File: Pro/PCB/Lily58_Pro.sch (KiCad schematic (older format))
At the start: 83 parts, among them J1 LED, J2 4PIN, J3 OLED, P1 i2c_pin, P2 i2c_pin, SW1 SW_PUSH, SW10 SW_PUSH, SW11 SW_PUSH, SW12 SW_PUSH, SW13 SW_PUSH, SW14 SW_PUSH, SW15 SW_PUSH, SW16 SW_PUSH, SW17 SW_PUSH, SW18 SW_PUSH, SW19 SW_PUSH, SW2 SW_PUSH, SW20 SW_PUSH, SW21 SW_PUSH, SW22 SW_PUSH, SW23 SW_PUSH, SW24 SW_PUSH, SW25 SW_PUSH, SW26 SW_PUSH, SW27 SW_PUSH, SW28 SW_PUSH, SW29 SW_PUSH, SW3 SW_PUSH, SW4 SW_PUSH, SW5 SW_PUSH, SW6 SW_PUSH, SW7 SW_PUSH, SW8 SW_PUSH, SW9 SW_PUSH, U1 ProMicro

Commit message: Add another switch.
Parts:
- added D30: D, Lily58-footprint:Diode_SOD123, symbol Lily58_Pro-rescue:D-Lily58-cache
- added SW30: SW_PUSH, Lily58-footprint:CherryMX_KailhLowProfile_Hotswap, symbol Lily58_Pro-rescue:SW_PUSH-Lily58-cache
- SW1, SW10, SW11, SW12, SW13, SW14, SW15, SW16, SW17, SW18, SW19, SW2, SW20, SW21, SW22, SW23, SW24, SW25, SW27, SW28, SW29, SW3, SW4, SW5, SW6, SW7, SW8, SW9: footprint Lily58-footprint:CherryMX_KailhLowProfile_Hotswap_edge_fixed -> Lily58-footprint:CherryMX_KailhLowProfile_Hotswap
- SW26: footprint Lily58-footprint:CherryMX_KailhLowProfile_Hotswap_edge_fixed -> Lily58-footprint:CherryMX_KailhLowProfile_Hotswap_1.5
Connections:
- net col0: now also SW30.1
- net row4: now also D30.1 (K)
- new net: D30.2 (A), SW30.2
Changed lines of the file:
@@
 F 0 "SW25" H 5800 5000 50  0000 C CNN
 F 1 "SW_PUSH" H 5800 4750 50  0000 C CNN
-F 2 "Lily58-footprint:CherryMX_KailhLowProfile_Hotswap_edge_fixed" H 5800 4850 50  0001 C CNN
+F 2 "Lily58-footprint:CherryMX_KailhLowProfile_Hotswap" H 5800 4850 50  0001 C CNN
 F 3 "" H 5800 4850 50  0000 C CNN
 	1    5800 4850
@@
 F 0 "SW26" H 6600 5000 50  0000 C CNN
 F 1 "SW_PUSH" H 6600 4750 50  0000 C CNN
-F 2 "Lily58-footprint:CherryMX_KailhLowProfile_Hotswap_edge_fixed" H 6600 4850 50  0001 C CNN
+F 2 "Lily58-footprint:CherryMX_KailhLowProfile_Hotswap_1.5" H 6600 4850 50  0001 C CNN
 F 3 "" H 6600 4850 50  0000 C CNN
 	1    6600 4850
@@
 F 0 "SW1" H 5800 2400 50  0000 C CNN
 F 1 "SW_PUSH" H 5800 2150 50  0000 C CNN
-F 2 "Lily58-footprint:CherryMX_KailhLowProfile_Hotswap_edge_fixed" H 5800 2250 50  0001 C CNN
+F 2 "Lily58-footprint:CherryMX_KailhLowProfile_Hotswap" H 5800 2250 50  0001 C CNN
 F 3 "" H 5800 2250 50  0000 C CNN
 	1    5800 2250
@@
 F 0 "SW2" H 6600 2400 50  0000 C CNN
 F 1 "SW_PUSH" H 6600 2150 50  0000 C CNN
-F 2 "Lily58-footprint:CherryMX_KailhLowProfile_Hotswap_edge_fixed" H 6600 2250 50  0001 C CNN
+F 2 "Lily58-footprint:CherryMX_KailhLowProfile_Hotswap" H 6600 2250 50  0001 C CNN
 F 3 "" H 6600 2250 50  0000 C CNN
 	1    6600 2250
@@
 F 0 "SW3" H 7400 2400 50  0000 C CNN
 F 1 "SW_PUSH" H 7400 2150 50  0000 C CNN
-F 2 "Lily58-footprint:CherryMX_KailhLowProfile_Hotswap_edge_fixed" H 7400 2250 50  0001 C CNN
+F 2 "Lily58-footprint:CherryMX_KailhLowProfile_Hotswap" H 7400 2250 50  0001 C CNN
 F 3 "" H 7400 2250 50  0000 C CNN
 	1    7400 2250
@@
 F 0 "SW4" H 8200 2400 50  0000 C CNN
 F 1 "SW_PUSH" H 8200 2150 50  0000 C CNN
-F 2 "Lily58-footprint:CherryMX_KailhLowProfile_Hotswap_edge_fixed" H 8200 2250 50  0001 C CNN
+F 2 "Lily58-footprint:CherryMX_KailhLowProfile_Hotswap" H 8200 2250 50  0001 C CNN
 F 3 "" H 8200 2250 50  0000 C CNN
 	1    8200 2250
@@
 F 0 "SW5" H 9000 2400 50  0000 C CNN
 F 1 "SW_PUSH" H 9000 2150 50  0000 C CNN
-F 2 "Lily58-footprint:CherryMX_KailhLowProfile_Hotswap_edge_fixed" H 9000 2250 50  0001 C CNN
+F 2 "Lily58-footprint:CherryMX_KailhLowProfile_Hotswap" H 9000 2250 50  0001 C CNN
 F 3 "" H 9000 2250 50  0000 C CNN
 	1    9000 2250
@@
 F 0 "SW6" H 9800 2400 50  0000 C CNN
 F 1 "SW_PUSH" H 9800 2200 50  0000 C CNN
-F 2 "Lily58-footprint:CherryMX_KailhLowProfile_Hotswap_edge_fixed" H 9800 2250 50  0001 C CNN
+F 2 "Lily58-footprint:CherryMX_KailhLowProfile_Hotswap" H 9800 2250 50  0001 C CNN
 F 3 "" H 9800 2250 50  0000 C CNN
 	1    9800 2250
@@
 F 0 "SW8" H 6600 3050 50  0000 C CNN
 F 1 "SW_PUSH" H 6600 2800 50  0000 C CNN
-F 2 "Lily58-footprint:CherryMX_KailhLowProfile_Hotswap_edge_fixed" H 6600 2900 50  0001 C CNN
+F 2 "Lily58-footprint:CherryMX_KailhLowProfile_Hotswap" H 6600 2900 50  0001 C CNN
 F 3 "" H 6600 2900 50  0000 C CNN
 	1    6600 2900
@@
 F 0 "SW9" H 7400 3050 50  0000 C CNN
 F 1 "SW_PUSH" H 7400 2800 50  0000 C CNN
-F 2 "Lily58-footprint:CherryMX_KailhLowProfile_Hotswap_edge_fixed" H 7400 2900 50  0001 C CNN
+F 2 "Lily58-footprint:CherryMX_KailhLowProfile_Hotswap" H 7400 2900 50  0001 C CNN
 F 3 "" H 7400 2900 50  0000 C CNN
 	1    7400 2900
@@
 F 0 "SW10" H 8200 3050 50  0000 C CNN
 F 1 "SW_PUSH" H 8200 2800 50  0000 C CNN
-F 2 "Lily58-footprint:CherryMX_KailhLowProfile_Hotswap_edge_fixed" H 8200 2900 50  0001 C CNN
+F 2 "Lily58-footprint:CherryMX_KailhLowProfile_Hotswap" H 8200 2900 50  0001 C CNN
 F 3 "" H 8200 2900 50  0000 C CNN
 	1    8200 2900
@@
 F 0 "SW11" H 9000 3050 50  0000 C CNN
 F 1 "SW_PUSH" H 9000 2800 50  0000 C CNN
-F 2 "Lily58-footprint:CherryMX_KailhLowProfile_Hotswap_edge_fixed" H 9000 2900 50  0001 C CNN
+F 2 "Lily58-footprint:CherryMX_KailhLowProfile_Hotswap" H 9000 2900 50  0001 C CNN
 F 3 "" H 9000 2900 50  0000 C CNN
 	1    9000 2900
@@
 F 0 "SW12" H 9800 3050 50  0000 C CNN
 F 1 "SW_PUSH" H 9800 2800 50  0000 C CNN
-F 2 "Lily58-footprint:CherryMX_KailhLowProfile_Hotswap_edge_fixed" H 9800 2900 50  0001 C CNN
+F 2 "Lily58-footprint:CherryMX_KailhLowProfile_Hotswap" H 9800 2900 50  0001 C CNN
 F 3 "" H 9800 2900 50  0000 C CNN
 	1    9800 2900
@@
 F 0 "SW7" H 5800 3050 50  0000 C CNN
 F 1 "SW_PUSH" H 5800 2800 50  0000 C CNN
-F 2 "Lily58-footprint:CherryMX_KailhLowProfile_Hotswap_edge_fixed" H 5800 2900 50  0001 C CNN
+F 2 "Lily58-footprint:CherryMX_KailhLowProfile_Hotswap" H 5800 2900 50  0001 C CNN
 F 3 "" H 5800 2900 50  0000 C CNN
 	1    5800 2900
@@
 F 0 "SW13" H 5800 3700 50  0000 C CNN
 F 1 "SW_PUSH" H 5800 3450 50  0000 C CNN
-F 2 "Lily58-footprint:CherryMX_KailhLowProfile_Hotswap_edge_fixed" H 5800 3550 50  0001 C CNN
+F 2 "Lily58-footprint:CherryMX_KailhLowProfile_Hotswap" H 5800 3550 50  0001 C CNN
 F 3 "" H 5800 3550 50  0000 C CNN
 	1    5800 3550
@@
 F 0 "SW14" H 6600 3700 50  0000 C CNN
 F 1 "SW_PUSH" H 6600 3450 50  0000 C CNN
-F 2 "Lily58-footprint:CherryMX_KailhLowProfile_Hotswap_edge_fixed" H 6600 3550 50  0001 C CNN
+F 2 "Lily58-footprint:CherryMX_KailhLowProfile_Hotswap" H 6600 3550 50  0001 C CNN
 F 3 "" H 6600 3550 50  0000 C CNN
 	1    6600 3550
@@
 F 0 "SW15" H 7400 3700 50  0000 C CNN
 F 1 "SW_PUSH" H 7400 3450 50  0000 C CNN
-F 2 "Lily58-footprint:CherryMX_KailhLowProfile_Hotswap_edge_fixed" H 7400 3550 50  0001 C CNN
+F 2 "Lily58-footprint:CherryMX_KailhLowProfile_Hotswap" H 7400 3550 50  0001 C CNN
 F 3 "" H 7400 3550 50  0000 C CNN
 	1    7400 3550
@@
 F 0 "SW16" H 8200 3700 50  0000 C CNN
 F 1 "SW_PUSH" H 8200 3450 50  0000 C CNN
-F 2 "Lily58-footprint:CherryMX_KailhLowProfile_Hotswap_edge_fixed" H 8200 3550 50  0001 C CNN
+F 2 "Lily58-footprint:CherryMX_KailhLowProfile_Hotswap" H 8200 3550 50  0001 C CNN
 F 3 "" H 8200 3550 50  0000 C CNN
 	1    8200 3550
@@
 F 0 "SW17" H 9000 3700 50  0000 C CNN
 F 1 "SW_PUSH" H 9000 3450 50  0000 C CNN
-F 2 "Lily58-footprint:CherryMX_KailhLowProfile_Hotswap_edge_fixed" H 9000 3550 50  0001 C CNN
+F 2 "Lily58-footprint:CherryMX_KailhLowProfile_Hotswap" H 9000 3550 50  0001 C CNN
 F 3 "" H 9000 3550 50  0000 C CNN
 	1    9000 3550
@@
 F 0 "SW18" H 9800 3700 50  0000 C CNN
 F 1 "SW_PUSH" H 9800 3450 50  0000 C CNN
-F 2 "Lily58-footprint:CherryMX_KailhLowProfile_Hotswap_edge_fixed" H 9800 3550 50  0001 C CNN
+F 2 "Lily58-footprint:CherryMX_KailhLowProfile_Hotswap" H 9800 3550 50  0001 C CNN
 F 3 "" H 9800 3550 50  0000 C CNN
 	1    9800 3550
@@
 F 0 "SW21" H 7400 4350 50  0000 C CNN
 F 1 "SW_PUSH" H 7400 4100 50  0000 C CNN
-F 2 "Lily58-footprint:CherryMX_KailhLowProfile_Hotswap_edge_fixed" H 7400 4200 50  0001 C CNN
+F 2 "Lily58-footprint:CherryMX_KailhLowProfile_Hotswap" H 7400 4200 50  0001 C CNN
 F 3 "" H 7400 4200 50  0000 C CNN
 	1    7400 4200
@@
 F 0 "SW22" H 8200 4350 50  0000 C CNN
 F 1 "SW_PUSH" H 8200 4100 50  0000 C CNN
-F 2 "Lily58-footprint:CherryMX_KailhLowProfile_Hotswap_edge_fixed" H 8200 4200 50  0001 C CNN
+F 2 "Lily58-footprint:CherryMX_KailhLowProfile_Hotswap" H 8200 4200 50  0001 C CNN
 F 3 "" H 8200 4200 50  0000 C CNN
 	1    8200 4200
@@
 F 0 "SW23" H 9000 4350 50  0000 C CNN
 F 1 "SW_PUSH" H 9000 4100 50  0000 C CNN
-F 2 "Lily58-footprint:CherryMX_KailhLowProfile_Hotswap_edge_fixed" H 9000 4200 50  0001 C CNN
+F 2 "Lily58-footprint:CherryMX_KailhLowProfile_Hotswap" H 9000 4200 50  0001 C CNN
 F 3 "" H 9000 4200 50  0000 C CNN
 	1    9000 4200
@@
 F 0 "SW24" H 9800 4350 50  0000 C CNN
 F 1 "SW_PUSH" H 9800 4100 50  0000 C CNN
-F 2 "Lily58-footprint:CherryMX_KailhLowProfile_Hotswap_edge_fixed" H 9800 4200 50  0001 C CNN
+F 2 "Lily58-footprint:CherryMX_KailhLowProfile_Hotswap" H 9800 4200 50  0001 C CNN
 F 3 "" H 9800 4200 50  0000 C CNN
 	1    9800 4200
@@
 F 0 "SW20" H 6600 4350 50  0000 C CNN
 F 1 "SW_PUSH" H 6600 4100 50  0000 C CNN
-F 2 "Lily58-footprint:CherryMX_KailhLowProfile_Hotswap_edge_fixed" H 6600 4200 50  0001 C CNN
+F 2 "Lily58-footprint:CherryMX_KailhLowProfile_Hotswap" H 6600 4200 50  0001 C CNN
 F 3 "" H 6600 4200 50  0000 C CNN
 	1    6600 4200
@@
 F 0 "SW19" H 5800 4350 50  0000 C CNN
 F 1 "SW_PUSH" H 5800 4100 50  0000 C CNN
-F 2 "Lily58-footprint:CherryMX_KailhLowProfile_Hotswap_edge_fixed" H 5800 4200 50  0001 C CNN
+F 2 "Lily58-footprint:CherryMX_KailhLowProfile_Hotswap" H 5800 4200 50  0001 C CNN
 F 3 "" H 5800 4200 50  0000 C CNN
 	1    5800 4200
@@
 F 0 "SW27" H 7400 5000 50  0000 C CNN
 F 1 "SW_PUSH" H 7400 4750 50  0000 C CNN
-F 2 "Lily58-footprint:CherryMX_KailhLowProfile_Hotswap_edge_fixed" H 7400 4850 50  0001 C CNN
+F 2 "Lily58-footprint:CherryMX_KailhLowProfile_Hotswap" H 7400 4850 50  0001 C CNN
 F 3 "" H 7400 4850 50  0000 C CNN
 	1    7400 4850
@@
 F 0 "SW28" H 8200 5000 50  0000 C CNN
 F 1 "SW_PUSH" H 8200 4750 50  0000 C CNN
-F 2 "Lily58-footprint:CherryMX_KailhLowProfile_Hotswap_edge_fixed" H 8200 4850 50  0001 C CNN
+F 2 "Lily58-footprint:CherryMX_KailhLowProfile_Hotswap" H 8200 4850 50  0001 C CNN
 F 3 "" H 8200 4850 50  0000 C CNN
 	1    8200 4850
@@
 F 0 "SW29" H 9000 5000 50  0000 C CNN
 F 1 "SW_PUSH" H 9000 4750 50  0000 C CNN
-F 2 "Lily58-footprint:CherryMX_KailhLowProfile_Hotswap_edge_fixed" H 9000 4850 50  0001 C CNN
+F 2 "Lily58-footprint:CherryMX_KailhLowProfile_Hotswap" H 9000 4850 50  0001 C CNN
 F 3 "" H 9000 4850 50  0000 C CNN
 	1    9000 4850
@@
 	3850 2400 4150 2400
 Connection ~ 3550 4550
+$Comp
+L Lily58_Pro-rescue:SW_PUSH-Lily58-cache SW30
+U 1 1 5D954F78
+P 9800 4850
+F 0 "SW30" H 9800 5000 50  0000 C CNN
+F 1 "SW_PUSH" H 9800 4750 50  0000 C CNN
+F 2 "Lily58-footprint:CherryMX_KailhLowProfile_Hotswap" H 9800 4850 50  0001 C CNN
+F 3 "" H 9800 4850 50  0000 C CNN
+	1    9800 4850
+	1    0    0    -1
+$EndComp
+$Comp
+L Lily58_Pro-rescue:D-Lily58-cache D30
+U 1 1 5D956FE1
+P 10100 5000
+F 0 "D30" V 10146 4921 50  0000 R CNN
+F 1 "D" V 10055 4921 50  0000 R CNN
+F 2 "Lily58-footprint:Diode_SOD123" H 10100 5000 50  0001 C CNN
+F 3 "" H 10100 5000 50  0001 C CNN
+	1    10100 5000
+	0    -1   -1   0
+$EndComp
+Wire Wire Line
+	9500 4200 9500 4850
+Connection ~ 9500 4200
+Wire Wire Line
+	9300 5150 10100 5150
+Connection ~ 9300 5150
 $EndSCHEMATC

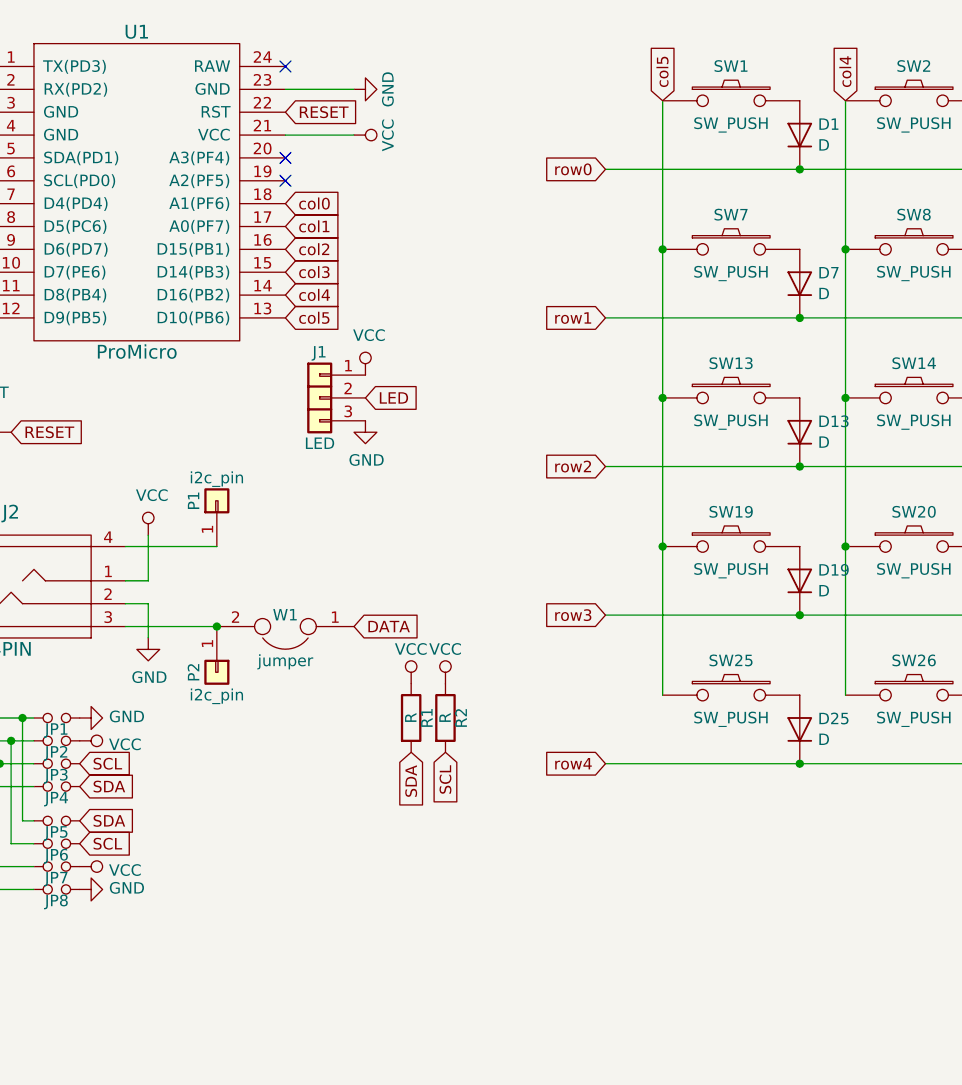
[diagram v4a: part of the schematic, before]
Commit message: Add rotary encoder, update pcb WIP.
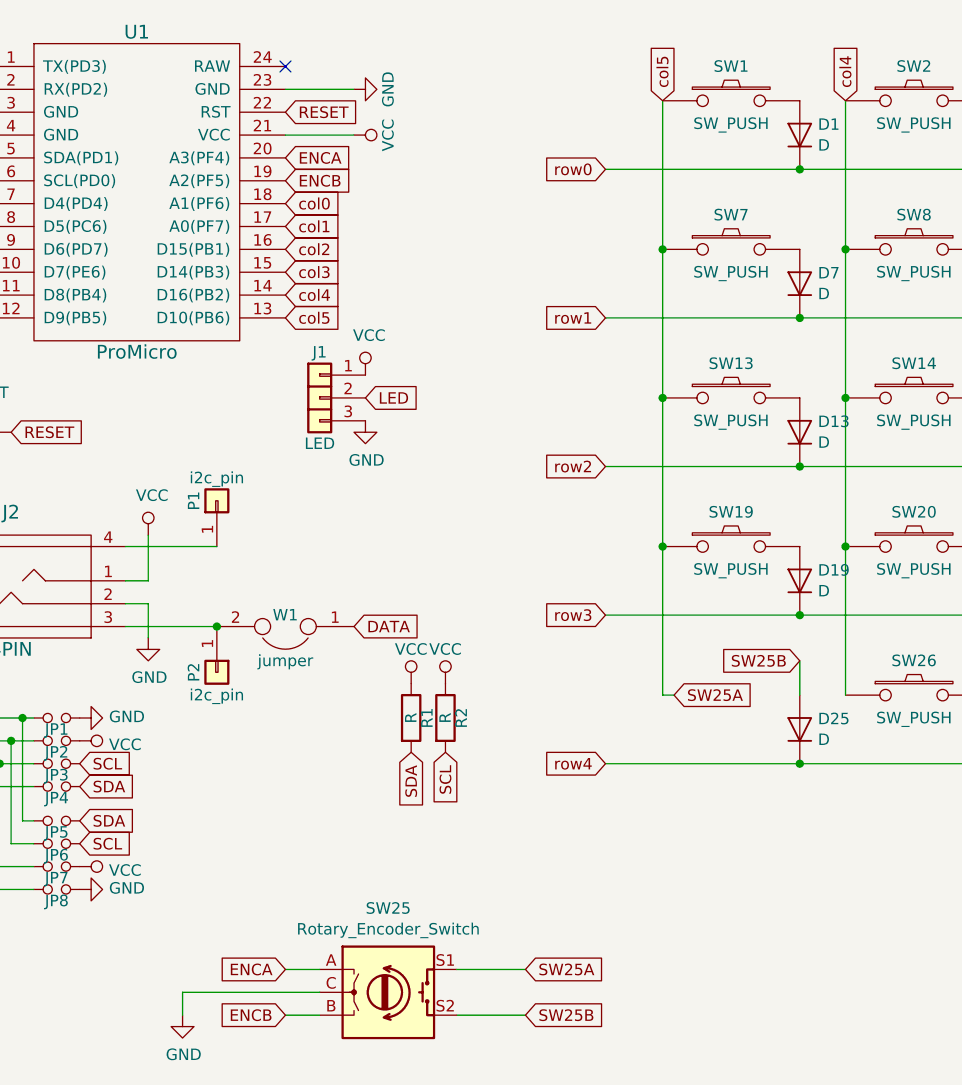
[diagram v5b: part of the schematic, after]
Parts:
- removed SW25: SW_PUSH, Lily58-footprint:CherryMX_KailhLowProfile_Hotswap, symbol Lily58_Pro-rescue:SW_PUSH-Lily58-cache
- added SW25: Rotary_Encoder_Switch, Lily58-footprint:RotaryEncoder_Alps_EC11E-Switch_Vertical_H20mm-keebio_modified, symbol Device:Rotary_Encoder_Switch
- J2: footprint Lily58-footprint:MJ-4PP-9 -> Lily58-footprint:MJ-4PP-9_rev3
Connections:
- net GND: now also SW25.C
- net ENCB: now reaches U1.19 (A2(PF5))
- net ENCB: now also SW25.B
- net ENCA: now reaches U1.20 (A3(PF4))
- net ENCA: now also SW25.A
- net SW25B: now reaches D25.2 (A)
- net SW25B: now also SW25.S2
- net col5 renamed SW25A
- net SW25A: now also SW25.S1
- no-connect marks 4 -> 2
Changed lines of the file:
@@
-$EndComp
-$Comp
-L Lily58_Pro-rescue:SW_PUSH-Lily58-cache SW25
-U 1 1 5B722503
-P 5800 4850
-F 0 "SW25" H 5800 5000 50  0000 C CNN
-F 1 "SW_PUSH" H 5800 4750 50  0000 C CNN
-F 2 "Lily58-footprint:CherryMX_KailhLowProfile_Hotswap" H 5800 4850 50  0001 C CNN
-F 3 "" H 5800 4850 50  0000 C CNN
-	1    5800 4850
-	1    0    0    -1
 $EndComp
 $Comp
@@
 Text GLabel 2550 2100 0    50   Input ~ 0
 LED
-NoConn ~ 3850 2600
 Text GLabel 2550 2600 0    50   Input ~ 0
 SCL
 Text GLabel 2550 2500 0    50   Input ~ 0
 SDA
-NoConn ~ 3850 2500
 Text GLabel 2550 2800 0    50   Input ~ 0
 row0
@@
 F 0 "J2" H 2650 4650 60  0000 C CNN
 F 1 "4PIN" H 2650 4050 60  0000 C CNN
-F 2 "Lily58-footprint:MJ-4PP-9" H 2700 4300 60  0001 C CNN
+F 2 "Lily58-footprint:MJ-4PP-9_rev3" H 2700 4300 60  0001 C CNN
 F 3 "" H 2700 4300 60  0000 C CNN
 	1    2700 4350
@@
 	9300 5150 10100 5150
 Connection ~ 9300 5150
+$Comp
+L Device:Rotary_Encoder_Switch SW25
+U 1 1 5DA04574
+P 4300 6150
+F 0 "SW25" H 4300 6517 50  0000 C CNN
+F 1 "Rotary_Encoder_Switch" H 4300 6426 50  0000 C CNN
+F 2 "Lily58-footprint:RotaryEncoder_Alps_EC11E-Switch_Vertical_H20mm-keebio_modified" H 4150 6310 50  0001 C CNN
+F 3 "~" H 4300 6410 50  0001 C CNN
+	1    4300 6150
+	1    0    0    -1
+$EndComp
+Text GLabel 4900 6050 2    50   Input ~ 0
+SW25A
+Text GLabel 4900 6250 2    50   Input ~ 0
+SW25B
+Wire Wire Line
+	4600 6050 4900 6050
+Wire Wire Line
+	4600 6250 4900 6250
+Text GLabel 5550 4850 2    50   Input ~ 0
+SW25A
+Text GLabel 6100 4700 0    50   Input ~ 0
+SW25B
+Wire Wire Line
+	6100 4700 6100 4850
+Wire Wire Line
+	5500 4850 5550 4850
+Text GLabel 3850 2500 2    50   Input ~ 0
+ENCA
+Text GLabel 3850 2600 2    50   Input ~ 0
+ENCB
+Text GLabel 3850 6050 0    50   Input ~ 0
+ENCA
+Text GLabel 3850 6250 0    50   Input ~ 0
+ENCB
+Wire Wire Line
+	3850 6250 4000 6250
+Wire Wire Line
+	3850 6050 4000 6050
+$Comp
+L power:GND #PWR0103
+U 1 1 5DA35FE6
+P 3400 6250
+F 0 "#PWR0103" H 3400 6000 50  0001 C CNN
+F 1 "GND" H 3405 6077 50  0000 C CNN
+F 2 "" H 3400 6250 50  0001 C CNN
+F 3 "" H 3400 6250 50  0001 C CNN
+	1    3400 6250
+	1    0    0    -1
+$EndComp
+Wire Wire Line
+	4000 6150 3400 6150
+Wire Wire Line
+	3400 6150 3400 6250
 $EndSCHEMATC

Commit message: Working on routing
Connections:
- net i2c_d: now reaches J2.3, P2.1 (Pin_1), W1.2
- net i2c_c: now reaches J2.4, P1.1 (Pin_1)
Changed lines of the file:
@@
 Wire Wire Line
 	3400 6150 3400 6250
+Text Label 3350 4550 0    50   ~ 0
+i2c_d
+Text Label 3300 4200 0    50   ~ 0
+i2c_c
 $EndSCHEMATC
